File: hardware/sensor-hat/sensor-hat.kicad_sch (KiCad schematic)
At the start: 62 parts, among them J10 probe socket, J11 data socket, J12 probe socket, J13 data socket, J14 probe socket, J16 I2C, J3 EZO pH probe, J4 EZO ORP probe, J5 EZO I2C probe, J6 1-Wire, J7 Contacts, J8 4-20 mA, J9 data socket, P1 J1 + J2, U1 EZO pH, U2 EZO ORP, U3 EZO I2C

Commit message: Lay out the PoolVeras V1.1 hat with the display, Atlas boards, and two buttons.
Socket 3 stays on the display I2C bus, and the screen shows pH, ORP, and water temperature.

Co-authored-by: Cursor <cursoragent@cursor.com>
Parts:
- added R29, R30: 10k, PCM_JLCPCB:R_0805, symbol Device:R
- added SW1, SW2: TS-1187A, Button_Switch_SMD:SW_Push_1P1T_XKB_TS-1187A, symbol Switch:SW_Push
- J16: footprint Connector_PinHeader_2.54mm:PinHeader_1x04_P2.54mm_Vertical -> Connector_PinSocket_2.54mm:PinSocket_1x04_P2.54mm_Vertical; Pin order 1 3V3, 2 GND, 3 SCL, 4 SDA. Pin 1 faces the fuse. Not fitte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 -> 1 GND, 2 3V3, 3 SCL, 4 SDA. Pin 1 is on the left. Female so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; now fitted; now in the parts list
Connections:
- net GND: now also J16.1 (GND), SW1.1, SW2.1; no longer J16.2 (GND)
- net V3OUT: now also J16.2 (3V3), R29.1, R30.1; no longer J16.1 (3V3)
- new net: P1.19 (BTN2  GPIO36), R30.2, SW2.2
- new net: P1.18 (BTN1  GPIO6), R29.2, SW1.2
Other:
- note added: "Buttons A and B sit at the USB-left corner. Each switch closes to ground. A 10k pulls the input up to the fused 3.3 V."
- note added: "EZO I2C. Switch this module to I2C before you plug it in. Pull-ups are fitted. J16 is the same bus: pin 1 GND toward the USB edge, then 3.3 V, SCL, and SDA toward the screws."
- note removed: "EZO I2C. Switch this module to I2C before you plug it in. Pull-ups are fitted. J16 is the same bus and is left empty."

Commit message: Record the hat after the display, button, and routing passes.
The board now keeps the packed Atlas modules, the external switch header, and the shorter front-side wiring.

Co-authored-by: Cursor <cursoragent@cursor.com>
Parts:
- added J17: external, Connector_PinHeader_2.54mm:PinHeader_1x04_P2.54mm_Vertical, symbol Connector_Generic:Conn_01x04
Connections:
- net GND: now also SW1.2, SW2.2, J17.2 (Pin_2), J17.4 (Pin_4); no longer SW1.1, SW2.1
- net BTN2: now reaches P1.19 (BTN2  GPIO6), R30.2
- net BTN2: now also SW2.1, J17.3 (Pin_3); no longer SW2.2
- net BTN1: now reaches P1.18 (BTN1  GPIO7), R29.2
- net BTN1: now also SW1.1, J17.1 (Pin_1); no longer SW1.2
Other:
- note added: "J17 brings SW1 and SW2 out for enclosure switches. Odd pins are the signals. Even pins are ground."
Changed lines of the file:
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@@
 	(symbol
 		(lib_id "Switch:SW_Push")
-		(at 161.29 542.29 180)
+		(at 161.29 542.29 0)
 		(unit 1)
 		(exclude_from_sim no)
@@
 			(effects (font (size 1.27 1.27)) (hide yes))
 		)
-		(property "Description" "pin 1 to GND, pin 2 to the GPIO. Silk A is SW1, silk B is SW2."
+		(property "Description" "pin 1 to the GPIO, pin 2 to GND. Silk A is SW1, silk B is SW2."
 			(at 161.29 542.29 0)
 			(effects (font (size 1.27 1.27)) (hide yes))
@@
 	(symbol
 		(lib_id "Switch:SW_Push")
-		(at 161.29 557.53 180)
+		(at 161.29 557.53 0)
 		(unit 1)
 		(exclude_from_sim no)
@@
 			(effects (font (size 1.27 1.27)) (hide yes))
 		)
-		(property "Description" "pin 1 to GND, pin 2 to the GPIO. Silk A is SW1, silk B is SW2."
+		(property "Description" "pin 1 to the GPIO, pin 2 to GND. Silk A is SW1, silk B is SW2."
 			(at 161.29 557.53 0)
 			(effects (font (size 1.27 1.27)) (hide yes))
@@
 		)
 	)
+	(symbol
+		(lib_id "Connector_Generic:Conn_01x04")
+		(at 185.42 542.29 0)
+		(unit 1)
+		(exclude_from_sim no)
+		(in_bom yes)
+		(on_board yes)
+		(dnp no)
+		(property "Reference" "J17"
+			(at 191.76999999999998 546.0999999999999 0)
+			(effects (font (size 1.27 1.27)))
+		)
+		(property "Value" "external"
+			(at 191.76999999999998 538.48 0)
+			(effects (font (size 1.27 1.27)))
+		)
+		(property "Footprint" "Connector_PinHeader_2.54mm:PinHeader_1x04_P2.54mm_Vertical"
+			(at 185.42 542.29 0)
+			(effects (font (size 1.27 1.27)) (hide yes))
+		)
+		(property "Datasheet" ""
+			(at 185.42 542.29 0)
+			(effects (font (size 1.27 1.27)) (hide yes))
+		)
+		(property "Description" "Pin 1 SW1, pin 2 GND, pin 3 SW2, pin 4 GND."
+			(at 185.42 542.29 0)
+			(effects (font (size 1.27 1.27)) (hide yes))
+		)
+		(pin "1"
+		)
+		(pin "2"
+		)
+		(pin "3"
+		)
+		(pin "4"
+		)
+		(instances
+			(project "sensor-hat"
+				(path "/108685f0-30ce-51b5-93f8-df7bf068f484"
+					(reference "J17")
+					(unit 1)
+				)
+			)
+		)
+	)
+	(symbol
+		(lib_id "power:GND")
+		(at 175.26 542.29 0)
+		(unit 1)
+		(exclude_from_sim no)
+		(in_bom no)
+		(on_board no)
+		(dnp no)
+		(property "Reference" "#PWR056"
+			(at 181.60999999999999 546.0999999999999 0)
+			(effects (font (size 1.27 1.27)) (hide yes))
+		)
+		(property "Value" "GND"
+			(at 181.60999999999999 538.48 0)
+			(effects (font (size 1.27 1.27)))
+		)
+		(property "Footprint" ""
+			(at 175.26 542.29 0)
+			(effects (font (size 1.27 1.27)) (hide yes))
+		)
+		(property "Datasheet" ""
+			(at 175.26 542.29 0)
+			(effects (font (size 1.27 1.27)) (hide yes))
+		)
+		(pin "1"
+		)
+		(instances
+			(project "sensor-hat"
+				(path "/108685f0-30ce-51b5-93f8-df7bf068f484"
+					(reference "#PWR056")
+					(unit 1)
+				)
+			)
+		)
+	)
+	(symbol
+		(lib_id "power:GND")
+		(at 175.26 547.37 0)
+		(unit 1)
+		(exclude_from_sim no)
+		(in_bom no)
+		(on_board no)
+		(dnp no)
+		(property "Reference" "#PWR057"
+			(at 181.60999999999999 551.18 0)
+			(effects (font (size 1.27 1.27)) (hide yes))
+		)
+		(property "Value" "GND"
+			(at 181.60999999999999 543.5600000000001 0)
+			(effects (font (size 1.27 1.27)))
+		)
+		(property "Footprint" ""
+			(at 175.26 547.37 0)
+			(effects (font (size 1.27 1.27)) (hide yes))
+		)
+		(property "Datasheet" ""
+			(at 175.26 547.37 0)
+			(effects (font (size 1.27 1.27)) (hide yes))
+		)
+		(pin "1"
+		)
+		(instances
+			(project "sensor-hat"
+				(path "/108685f0-30ce-51b5-93f8-df7bf068f484"
+					(reference "#PWR057")
+					(unit 1)
+				)
+			)
+		)
+	)
 	(wire
 		(pts
@@
 		(stroke (width 0) (type solid))
 	)
+	(wire
+		(pts
+			(xy 180.34 539.75)
+			(xy 175.26 539.75)
+		)
+		(stroke (width 0) (type solid))
+	)
+	(wire
+		(pts
+			(xy 180.34 542.29)
+			(xy 175.26 542.29)
+		)
+		(stroke (width 0) (type solid))
+	)
+	(wire
+		(pts
+			(xy 180.34 544.83)
+			(xy 175.26 544.83)
+		)
+		(stroke (width 0) (type solid))
+	)
+	(wire
+		(pts
+			(xy 180.34 547.37)
+			(xy 175.26 547.37)
+		)
+		(stroke (width 0) (type solid))
+	)
 	(label "SIG1"
 		(at 185.42 85.09 0)
@@
 		(effects (font (size 1.27 1.27)) (justify left bottom))
 	)
+	(label "BTN1"
+		(at 146.05 542.29 0)
+		(effects (font (size 1.27 1.27)) (justify left bottom))
+	)
+	(label "BTN2"
+		(at 146.05 557.53 0)
+		(effects (font (size 1.27 1.27)) (justify left bottom))
+	)
+	(label "BTN1"
+		(at 175.26 539.75 0)
+		(effects (font (size 1.27 1.27)) (justify right bottom))
+	)
+	(label "BTN2"
+		(at 175.26 544.83 0)
+		(effects (font (size 1.27 1.27)) (justify right bottom))
+	)
 	(text "P1 is J1 and J2 together: the Pico sockets on the Waveshare."
 		(exclude_from_sim no)
@@
 		(effects (font (size 1.2 1.2)))
 	)
+	(text "J17 brings SW1 and SW2 out for enclosure switches. Odd pins are the signals. Even pins are ground."
+		(exclude_from_sim no)
+		(at 130 575.53 0)
+		(effects (font (size 1.2 1.2)))
+	)

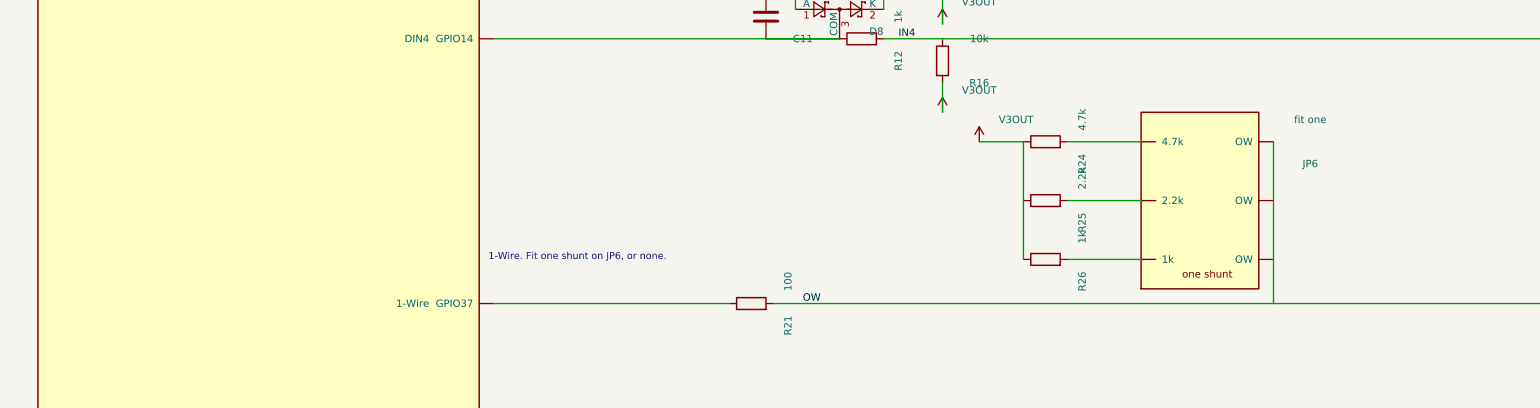
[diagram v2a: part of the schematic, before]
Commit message: Match the controller to the finished hat pinout and the 1-Wire slide switch.
Co-authored-by: Cursor <cursoragent@cursor.com>
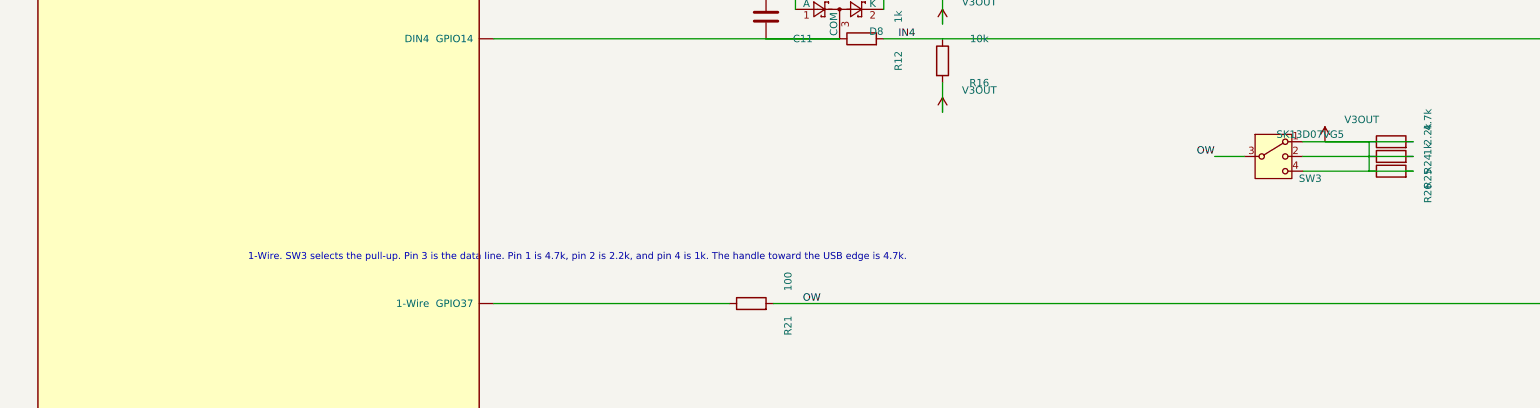
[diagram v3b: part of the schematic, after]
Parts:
- removed JP6: fit one, Connector_PinHeader_2.54mm:PinHeader_2x03_P2.54mm_Vertical, symbol sensor-hat:JP6
- added SW3: SK13D07VG5, SensorHat:SW_SK13D07VG5, symbol Switch:SW_SP3T
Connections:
- net OW: now also SW3.3
- net V3OUT: now also R24.2, SW3.1
- net at R26.2: now also SW3.4
- net at R25.2: now also SW3.2
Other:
- note added: "1-Wire. SW3 selects the pull-up. Pin 3 is the data line. Pin 1 is 4.7k, pin 2 is 2.2k, and pin 4 is 1k. The handle toward the USB edge is 4.7k."
- note removed: "1-Wire. Fit one shunt on JP6, or none."
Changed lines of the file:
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@@
 	)
 	(symbol
-		(lib_id "sensor-hat:JP6")
-		(at 250.19 240.03 0)
+		(lib_id "Switch:SW_SP3T")
+		(at 250.19 242.57 0)
 		(unit 1)
 		(exclude_from_sim no)
@@
 		(on_board yes)
 		(dnp no)
-		(property "Reference" "JP6"
-			(at 256.54 243.84 0)
-			(effects (font (size 1.27 1.27)))
-		)
-		(property "Value" "fit one"
-			(at 256.54 236.22 0)
-			(effects (font (size 1.27 1.27)))
-		)
-		(property "Footprint" "Connector_PinHeader_2.54mm:PinHeader_2x03_P2.54mm_Vertical"
-			(at 250.19 240.03 0)
-			(effects (font (size 1.27 1.27)) (hide yes))
-		)
-		(property "Datasheet" ""
-			(at 250.19 240.03 0)
-			(effects (font (size 1.27 1.27)) (hide yes))
-		)
-		(property "Description" "Fit ONE shunt: pins 1-2 are 4.7k, 3-4 are 2.2k, 5-6 are 1k"
-			(at 250.19 240.03 0)
-			(effects (font (size 1.27 1.27)) (hide yes))
+		(property "Reference" "SW3"
+			(at 256.54 246.38 0)
+			(effects (font (size 1.27 1.27)))
+		)
+		(property "Value" "SK13D07VG5"
+			(at 256.54 238.76 0)
+			(effects (font (size 1.27 1.27)))
+		)
+		(property "Footprint" "SensorHat:SW_SK13D07VG5"
+			(at 250.19 242.57 0)
+			(effects (font (size 1.27 1.27)) (hide yes))
+		)
+		(property "Datasheet" ""
+			(at 250.19 242.57 0)
+			(effects (font (size 1.27 1.27)) (hide yes))
+		)
+		(property "LCSC" "C393948"
+			(at 250.19 242.57 0)
+			(effects (font (size 1.27 1.27)) (hide yes))
+		)
+		(property "Description" "SHOU HAN SK13D07VG5, right-angle SP3T. Pin 3 is common (1-Wire data). Pin 1 is 4.7k, pin 2 is 2.2k, pin 4 is 1k."
+			(at 250.19 242.57 0)
+			(effects (font (size 1.27 1.27)) (hide yes))
+		)
+		(pin "1"
 		)
 		(pin "2"
 		)
+		(pin "3"
+		)
 		(pin "4"
 		)
-		(pin "6"
-		)
-		(pin "1"
-		)
-		(pin "3"
-		)
-		(pin "5"
-		)
-		(instances
-			(project "sensor-hat"
-				(path "/108685f0-30ce-51b5-93f8-df7bf068f484"
-					(reference "JP6")
+		(instances
+			(project "sensor-hat"
+				(path "/108685f0-30ce-51b5-93f8-df7bf068f484"
+					(reference "SW3")
 					(unit 1)
 				)
@@
 	(symbol
 		(lib_id "Device:R")
-		(at 210.82 240.03 90)
+		(at 270.51 240.03 90)
 		(unit 1)
 		(exclude_from_sim no)
@@
 		(dnp no)
 		(property "Reference" "R24"
-			(at 217.17 243.84 0)
+			(at 276.86 243.84 0)
 			(effects (font (size 1.27 1.27)))
 		)
 		(property "Value" "4.7k"
-			(at 217.17 236.22 0)
+			(at 276.86 236.22 0)
 			(effects (font (size 1.27 1.27)))
 		)
 		(property "Footprint" "PCM_JLCPCB:R_0805"
-			(at 210.82 240.03 0)
-			(effects (font (size 1.27 1.27)) (hide yes))
-		)
-		(property "Datasheet" ""
-			(at 210.82 240.03 0)
+			(at 270.51 240.03 0)
+			(effects (font (size 1.27 1.27)) (hide yes))
+		)
+		(property "Datasheet" ""
+			(at 270.51 240.03 0)
 			(effects (font (size 1.27 1.27)) (hide yes))
 		)
 		(property "LCSC" "C17673"
-			(at 210.82 240.03 0)
+			(at 270.51 240.03 0)
 			(effects (font (size 1.27 1.27)) (hide yes))
 		)
 		(property "Tolerance" "1%"
-			(at 210.82 240.03 0)
+			(at 270.51 240.03 0)
 			(effects (font (size 1.27 1.27)) (hide yes))
 		)
@@
 	(symbol
 		(lib_id "Device:R")
-		(at 210.82 250.19 90)
+		(at 270.51 242.57 90)
 		(unit 1)
 		(exclude_from_sim no)
@@
 		(dnp no)
 		(property "Reference" "R25"
-			(at 217.17 254.0 0)
+			(at 276.86 246.38 0)
 			(effects (font (size 1.27 1.27)))
 		)
 		(property "Value" "2.2k"
-			(at 217.17 246.38 0)
+			(at 276.86 238.76 0)
 			(effects (font (size 1.27 1.27)))
 		)
 		(property "Footprint" "PCM_JLCPCB:R_0805"
-			(at 210.82 250.19 0)
-			(effects (font (size 1.27 1.27)) (hide yes))
-		)
-		(property "Datasheet" ""
-			(at 210.82 250.19 0)
+			(at 270.51 242.57 0)
+			(effects (font (size 1.27 1.27)) (hide yes))
+		)
+		(property "Datasheet" ""
+			(at 270.51 242.57 0)
 			(effects (font (size 1.27 1.27)) (hide yes))
 		)
 		(property "LCSC" "C17520"
-			(at 210.82 250.19 0)
+			(at 270.51 242.57 0)
 			(effects (font (size 1.27 1.27)) (hide yes))
 		)
 		(property "Tolerance" "1%"
-			(at 210.82 250.19 0)
+			(at 270.51 242.57 0)
 			(effects (font (size 1.27 1.27)) (hide yes))
 		)
@@
 	(symbol
 		(lib_id "Device:R")
-		(at 210.82 260.35 90)
+		(at 270.51 245.11 90)
 		(unit 1)
 		(exclude_from_sim no)
@@
 		(dnp no)
 		(property "Reference" "R26"
-			(at 217.17 264.16 0)
+			(at 276.86 248.92000000000002 0)
 			(effects (font (size 1.27 1.27)))
 		)
 		(property "Value" "1k"
-			(at 217.17 256.54 0)
+			(at 276.86 241.3 0)
 			(effects (font (size 1.27 1.27)))
 		)
 		(property "Footprint" "PCM_JLCPCB:R_0805"
-			(at 210.82 260.35 0)
-			(effects (font (size 1.27 1.27)) (hide yes))
-		)
-		(property "Datasheet" ""
-			(at 210.82 260.35 0)
+			(at 270.51 245.11 0)
+			(effects (font (size 1.27 1.27)) (hide yes))
+		)
+		(property "Datasheet" ""
+			(at 270.51 245.11 0)
 			(effects (font (size 1.27 1.27)) (hide yes))
 		)
 		(property "LCSC" "C17513"
-			(at 210.82 260.35 0)
+			(at 270.51 245.11 0)
 			(effects (font (size 1.27 1.27)) (hide yes))
 		)
 		(property "Tolerance" "1%"
-			(at 210.82 260.35 0)
+			(at 270.51 245.11 0)
 			(effects (font (size 1.27 1.27)) (hide yes))
 		)
@@
 	(symbol
 		(lib_id "power:V3OUT")
-		(at 199.39 240.03 0)
+		(at 259.08 240.03 0)
 		(unit 1)
 		(exclude_from_sim no)
@@
 		(dnp no)
 		(property "Reference" "#PWR041"
-			(at 205.73999999999998 243.84 0)
+			(at 265.43 243.84 0)
 			(effects (font (size 1.27 1.27)) (hide yes))
 		)
 		(property "Value" "V3OUT"
-			(at 205.73999999999998 236.22 0)
+			(at 265.43 236.22 0)
 			(effects (font (size 1.27 1.27)))
 		)
 		(property "Footprint" ""
-			(at 199.39 240.03 0)
-			(effects (font (size 1.27 1.27)) (hide yes))
-		)
-		(property "Datasheet" ""
-			(at 199.39 240.03 0)
+			(at 259.08 240.03 0)
+			(effects (font (size 1.27 1.27)) (hide yes))
+		)
+		(property "Datasheet" ""
+			(at 259.08 240.03 0)
 			(effects (font (size 1.27 1.27)) (hide yes))
 		)
@@
 	(wire
 		(pts
-			(xy 250.19 240.03)
-			(xy 250.19 250.19)
-		)
-		(stroke (width 0) (type solid))
-	)
-	(wire
-		(pts
-			(xy 250.19 250.19)
-			(xy 250.19 260.35)
-		)
-		(stroke (width 0) (type solid))
-	)
-	(wire
-		(pts
-			(xy 250.19 260.35)
-			(xy 250.19 267.97)
-		)
-		(stroke (width 0) (type solid))
-	)
-	(wire
-		(pts
-			(xy 214.63 240.03)
-			(xy 227.33 240.03)
-		)
-		(stroke (width 0) (type solid))
-	)
-	(wire
-		(pts
-			(xy 214.63 250.19)
-			(xy 227.33 250.19)
-		)
-		(stroke (width 0) (type solid))
-	)
-	(wire
-		(pts
-			(xy 214.63 260.35)
-			(xy 227.33 260.35)
-		)
-		(stroke (width 0) (type solid))
-	)
-	(wire
-		(pts
-			(xy 207.01 240.03)
-			(xy 207.01 250.19)
-		)
-		(stroke (width 0) (type solid))
-	)
-	(wire
-		(pts
-			(xy 207.01 250.19)
-			(xy 207.01 260.35)
-		)
-		(stroke (width 0) (type solid))
-	)
-	(wire
-		(pts
-			(xy 207.01 240.03)
-			(xy 199.39 240.03)
+			(xy 245.11 242.57)
+			(xy 240.03 242.57)
+		)
+		(stroke (width 0) (type solid))
+	)
+	(wire
+		(pts
+			(xy 274.32 240.03)
+			(xy 255.27 240.03)
+		)
+		(stroke (width 0) (type solid))
+	)
+	(wire
+		(pts
+			(xy 274.32 242.57)
+			(xy 255.27 242.57)
+		)
+		(stroke (width 0) (type solid))
+	)
+	(wire
+		(pts
+			(xy 274.32 245.11)
+			(xy 255.27 245.11)
+		)
+		(stroke (width 0) (type solid))
+	)
+	(wire
+		(pts
+			(xy 266.7 240.03)
+			(xy 266.7 242.57)
+		)
+		(stroke (width 0) (type solid))
+	)
+	(wire
+		(pts
+			(xy 266.7 242.57)
+			(xy 266.7 245.11)
+		)
+		(stroke (width 0) (type solid))
+	)
+	(wire
+		(pts
+			(xy 266.7 240.03)
+			(xy 259.08 240.03)
 		)
 		(stroke (width 0) (type solid))
@@
 		(effects (font (size 1.27 1.27)) (justify left bottom))
 	)
+	(label "OW"
+		(at 240.03 242.57 0)
+		(effects (font (size 1.27 1.27)) (justify right bottom))
+	)
 	(label "PH_PRB"
 		(at 253.37 382.27 0)
@@
 		(effects (font (size 1.2 1.2)))
 	)
-	(text "1-Wire. Fit one shunt on JP6, or none."
+	(text "1-Wire. SW3 selects the pull-up. Pin 3 is the data line. Pin 1 is 4.7k, pin 2 is 2.2k, and pin 4 is 1k. The handle toward the USB edge is 4.7k."
 		(exclude_from_sim no)
 		(at 130 259.97 0)
